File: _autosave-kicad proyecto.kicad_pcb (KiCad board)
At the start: 4 copper layers, 100 x 100 mm, 46 parts, among them J1 USB_B, J2 UART, Q1 MMBT3904, SW1 SW_SPST, SW2 SW_SPST, SW3 SW_SPST, U1 NE555D, U2 NE555D, U3 FT232RL, U4 LM741, U5 4040, U6 4040

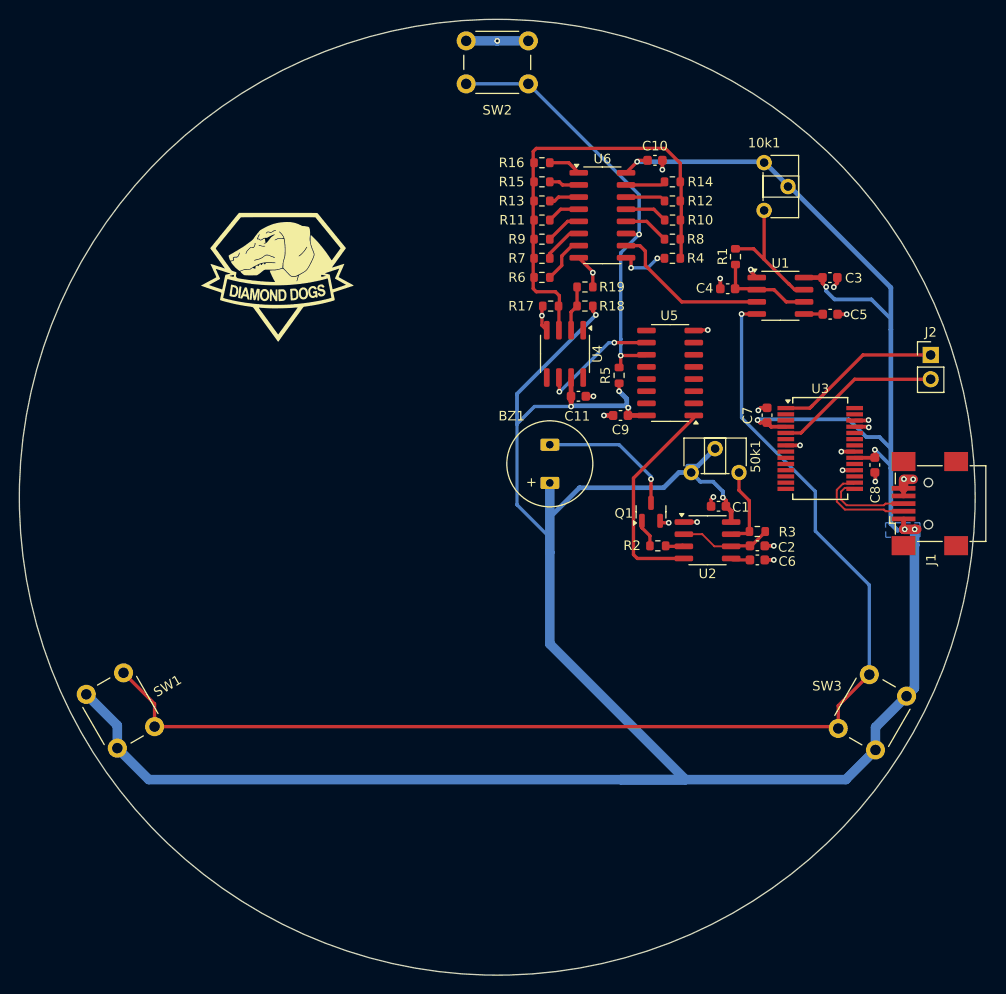
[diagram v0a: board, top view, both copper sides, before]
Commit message: routeo de una pista al plano superior en vez de vias
movi una pista al plano superior y modifique el ancho de algunas pistas de power, agregue stitching al resto de la placa
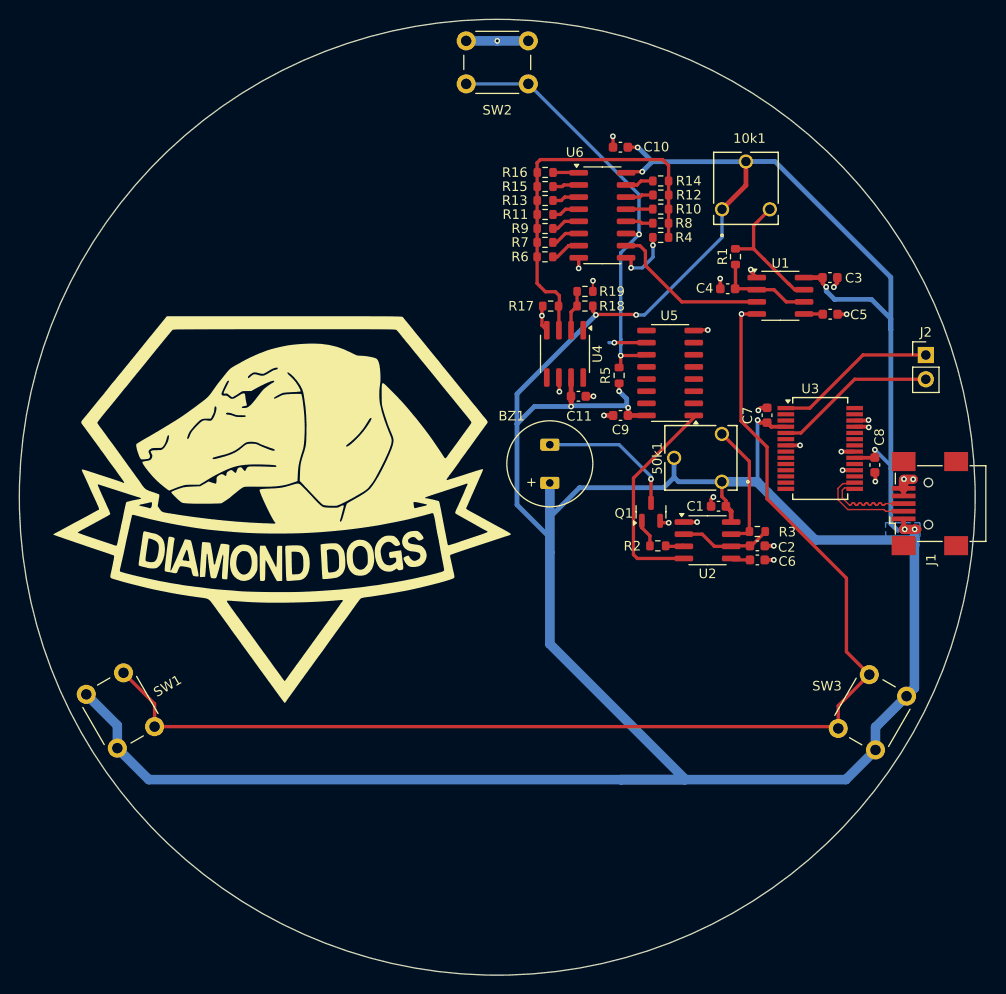
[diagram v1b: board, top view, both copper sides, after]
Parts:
- 10k1, 50k1: footprint Potentiometer_THT:Potentiometer_ACP_CA6-H2,5_Horizontal -> pretty:601030
- moved G*** 24.3 mm to (122.5, 106.3)
- moved 10k1 6.57 mm to (168.5, 74.9)
- moved C10 3.87 mm to (157.9, 68.4), turned to 180 degrees
- moved 50k1 3.35 mm to (168.5, 103.4)
- moved R4 2.50 mm to (162.1, 77.8)
- moved R6 2.18 mm to (150.0, 79.8)
- moved R8 2.07 mm to (162.1, 76.3)
- moved R7 1.70 mm to (150.0, 78.3)
- moved R10 1.69 mm to (162.1, 74.9)
- moved R12 1.36 mm to (162.1, 73.4)
- moved R14 1.23 mm to (162.1, 71.9)
- moved R9 1.16 mm to (150.0, 76.9)
- moved R16 1.07 mm to (150.0, 71.0)
- moved R11 0.67 mm to (150.0, 75.4)
- moved R15 0.60 mm to (150.0, 72.5)
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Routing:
- net +5V: track 340.4 -> 383.4 mm, vias 11 -> 12
- net Net-(U5-CLK): track 12.7 -> 5.48 mm
- net Net-(U4-+): track 47.1 -> 40.8 mm
- net Net-(U2-DIS): track 9.51 -> 14.3 mm
- net Net-(U6-Q8): track 4.80 -> 2.88 mm
- net Net-(U6-Q1): track 4.99 -> 3.19 mm
- net Net-(U6-Q7): track 4.51 -> 2.81 mm
- net Net-(U6-Q2): track 4.39 -> 3.09 mm
- net Net-(U6-Q9): track 4.19 -> 2.90 mm
- net GND: track 39.0 -> 37.7 mm, vias 25 -> 78
- net Net-(U6-Q10): track 4.16 -> 2.98 mm
- net /USB_D P: track 9.32 -> 10.4 mm
- net Net-(U6-Q3): track 3.80 -> 3.01 mm
- net Net-(U6-Q11): track 3.46 -> 2.70 mm
- net Net-(J2-Pin_1): track 17.7 -> 17.0 mm
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
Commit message: BOM actualizado en el csv
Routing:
- net Net-(U5-CLK): track 5.48 -> 11.7 mm, vias 2 -> 0
- net Net-(SW1-B): vias 1 -> 0
- net GND: vias 78 -> 107
